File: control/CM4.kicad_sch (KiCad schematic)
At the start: 1 part

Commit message: Cleanup/organization
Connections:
- net +5V: now reaches Module1.77 (+5v_(Input)), Module1.79 (+5v_(Input)), Module1.81 (+5v_(Input)), Module1.83 (+5v_(Input)), Module1.85 (+5v_(Input)), Module1.87 (+5v_(Input))
- net +3V3: now reaches Module1.84 (+3.3v_(Output)), Module1.86 (+3.3v_(Output))
- net +1V8: now reaches Module1.88 (+1.8v_(Output)), Module1.90 (+1.8v_(Output))
- no-connect marks 73 -> 86

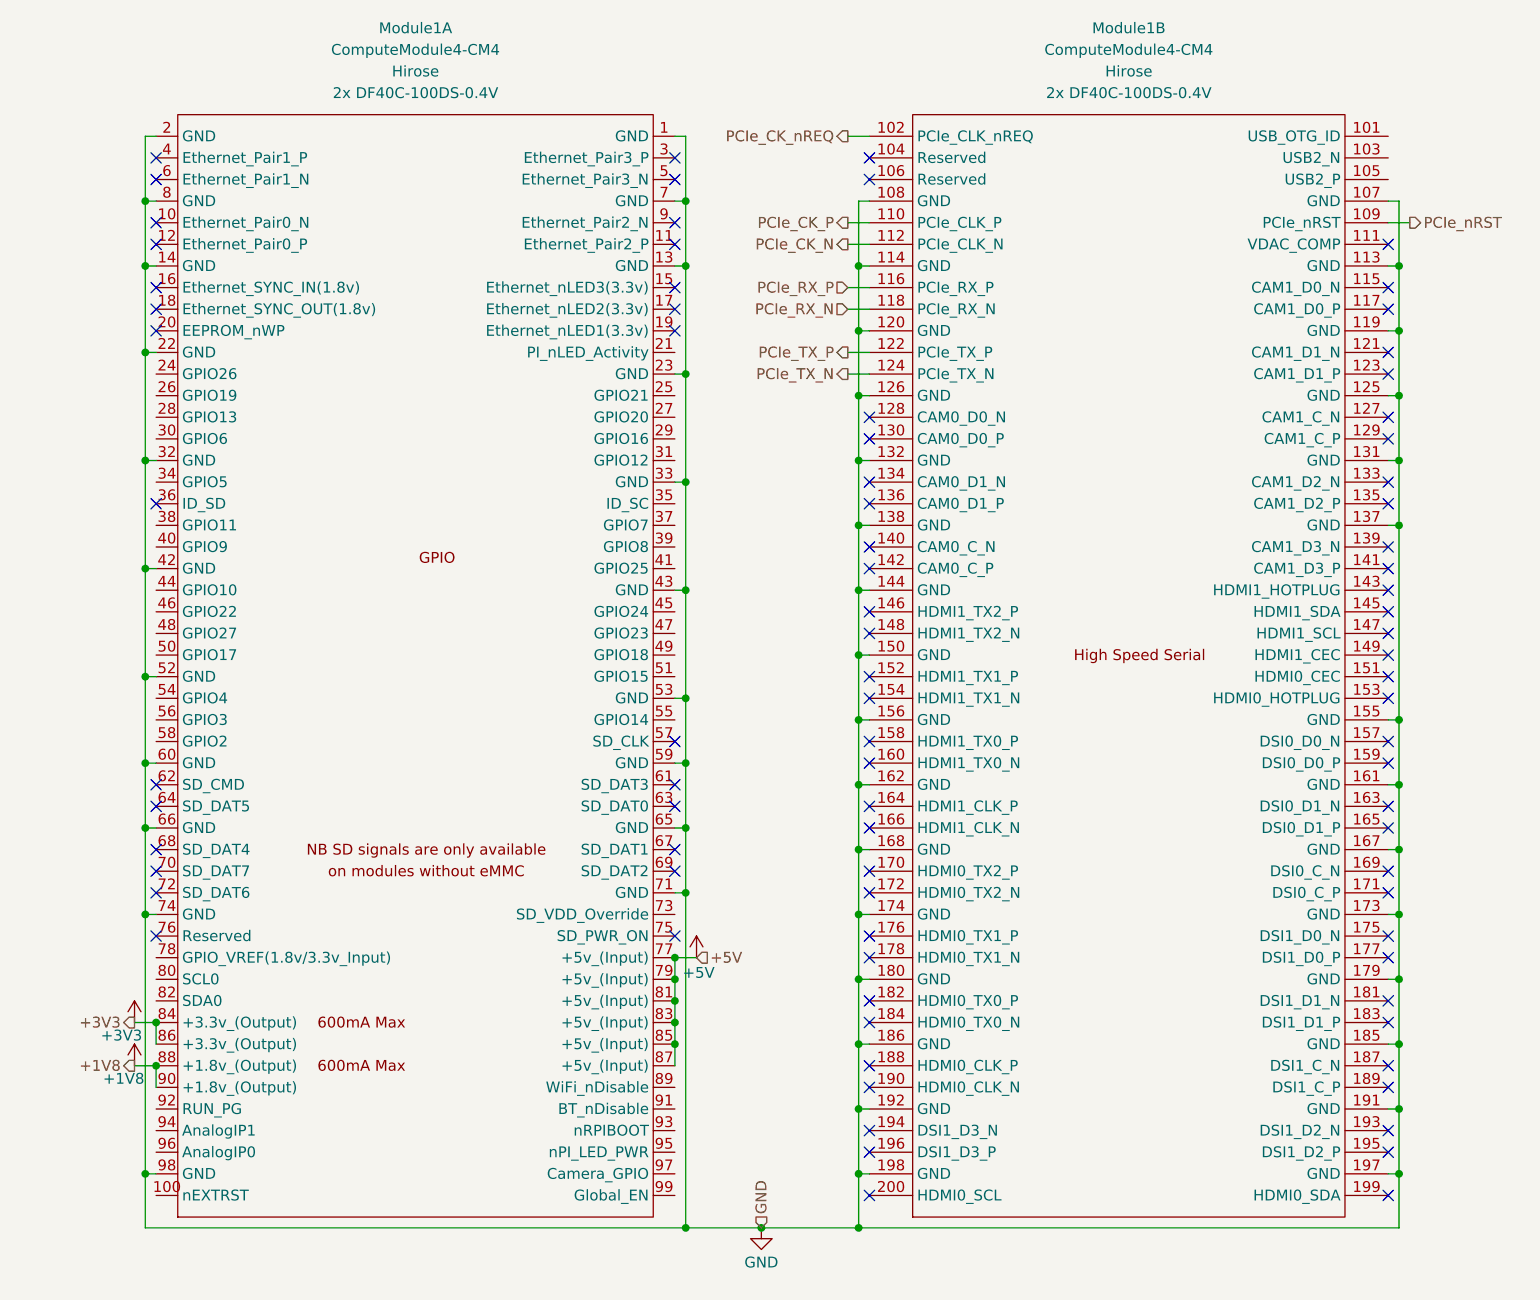
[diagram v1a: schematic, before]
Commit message: Component selection and BME280 cleanup
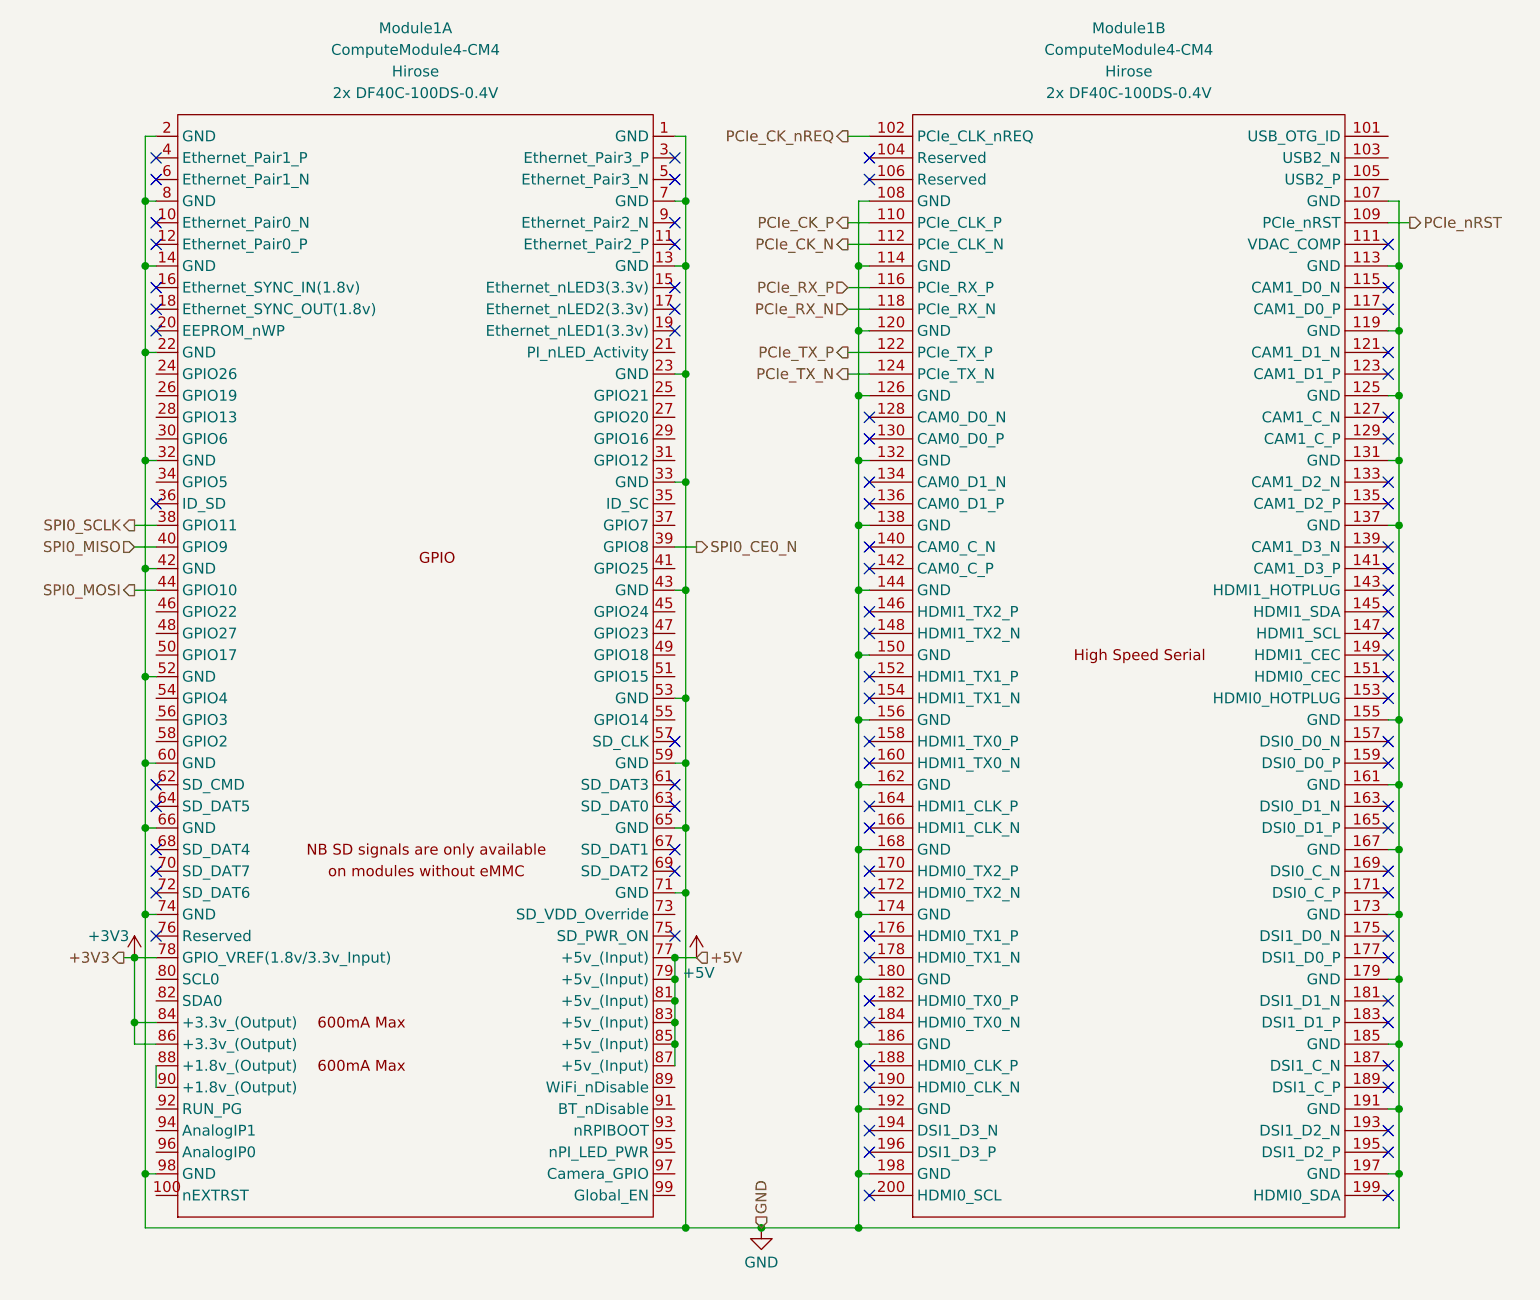
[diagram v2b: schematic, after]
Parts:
- Module1: PN CM4104000 -> SC0671
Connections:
- net +3V3: now also Module1.78 (GPIO_VREF(1.8v/3.3v_Input))
- net SPI0_SCLK: now reaches Module1.38 (GPIO11)
- net SPI0_CE0_N: now reaches Module1.39 (GPIO8)
- net SPI0_MISO: now reaches Module1.40 (GPIO9)
- net SPI0_MOSI: now reaches Module1.44 (GPIO10)
- net +1V8: no longer names the net of Module1.88 (+1.8v_(Output)), Module1.90 (+1.8v_(Output))
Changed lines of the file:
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@@
+	)
+	(junction
+		(at 40.64 133.35)
+		(diameter 0)
+		(color 0 0 0 0)
 	)
 	(junction
@@
 	)
 	(junction
-		(at 43.18 133.35)
-		(diameter 0)
-		(color 0 0 0 0)
-	)
-	(junction
 		(at 125.73 44.45)
 		(diameter 0)
@@
 	)
 	(junction
+		(at 40.64 125.73)
+		(diameter 0)
+		(color 0 0 0 0)
+	)
+	(junction
 		(at 105.41 95.25)
 		(diameter 0)
@@
 	)
 	(junction
-		(at 43.18 138.43)
-		(diameter 0)
-		(color 0 0 0 0)
-	)
-	(junction
 		(at 41.91 151.13)
 		(diameter 0)
@@
 	(wire
 		(pts
+			(xy 40.64 133.35) (xy 43.18 133.35)
+		)
+		(stroke
+			(width 0)
+			(type default)
+		)
+	)
+	(wire
+		(pts
 			(xy 104.14 95.25) (xy 105.41 95.25)
 		)
@@
 	(wire
 		(pts
+			(xy 40.64 82.55) (xy 43.18 82.55)
+		)
+		(stroke
+			(width 0)
+			(type default)
+		)
+	)
+	(wire
+		(pts
 			(xy 104.14 44.45) (xy 105.41 44.45)
 		)
@@
 	(wire
 		(pts
+			(xy 39.37 125.73) (xy 40.64 125.73)
+		)
+		(stroke
+			(width 0)
+			(type default)
+		)
+	)
+	(wire
+		(pts
 			(xy 189.23 59.69) (xy 187.96 59.69)
 		)
@@
 	(wire
 		(pts
+			(xy 40.64 125.73) (xy 43.18 125.73)
+		)
+		(stroke
+			(width 0)
+			(type default)
+		)
+	)
+	(wire
+		(pts
 			(xy 41.91 157.48) (xy 41.91 151.13)
 		)
@@
 	(wire
 		(pts
-			(xy 41.91 151.13) (xy 41.91 120.65)
-		)
-		(stroke
-			(width 0)
-			(type default)
-		)
-	)
-	(wire
-		(pts
 			(xy 114.3 157.48) (xy 105.41 157.48)
 		)
@@
 	(wire
 		(pts
+			(xy 40.64 77.47) (xy 43.18 77.47)
+		)
+		(stroke
+			(width 0)
+			(type default)
+		)
+	)
+	(wire
+		(pts
 			(xy 127 120.65) (xy 125.73 120.65)
 		)
@@
 	(wire
 		(pts
-			(xy 40.64 138.43) (xy 43.18 138.43)
-		)
-		(stroke
-			(width 0)
-			(type default)
-		)
-	)
-	(wire
-		(pts
 			(xy 125.73 67.31) (xy 125.73 59.69)
 		)
@@
 	(wire
 		(pts
+			(xy 104.14 77.47) (xy 106.68 77.47)
+		)
+		(stroke
+			(width 0)
+			(type default)
+		)
+	)
+	(wire
+		(pts
 			(xy 125.73 143.51) (xy 127 143.51)
 		)
@@
 	(wire
 		(pts
+			(xy 40.64 74.93) (xy 43.18 74.93)
+		)
+		(stroke
+			(width 0)
+			(type default)
+		)
+	)
+	(wire
+		(pts
 			(xy 104.14 135.89) (xy 104.14 138.43)
 		)
@@
 	(wire
 		(pts
-			(xy 43.18 133.35) (xy 43.18 135.89)
+			(xy 40.64 133.35) (xy 40.64 135.89)
 		)
 		(stroke
@@
 	(wire
 		(pts
+			(xy 40.64 135.89) (xy 43.18 135.89)
+		)
+		(stroke
+			(width 0)
+			(type default)
+		)
+	)
+	(wire
+		(pts
 			(xy 125.73 143.51) (xy 125.73 151.13)
 		)
@@
 	(wire
 		(pts
-			(xy 40.64 133.35) (xy 43.18 133.35)
-		)
-		(stroke
-			(width 0)
-			(type default)
-		)
-	)
-	(wire
-		(pts
 			(xy 127 128.27) (xy 125.73 128.27)
 		)
@@
 	(wire
 		(pts
+			(xy 41.91 120.65) (xy 41.91 151.13)
+		)
+		(stroke
+			(width 0)
+			(type default)
+		)
+	)
+	(wire
+		(pts
 			(xy 125.73 74.93) (xy 125.73 67.31)
 		)
@@
 		(pts
 			(xy 105.41 36.83) (xy 104.14 36.83)
+		)
+		(stroke
+			(width 0)
+			(type default)
+		)
+	)
+	(wire
+		(pts
+			(xy 40.64 133.35) (xy 40.64 125.73)
 		)
 		(stroke
@@
 		)
 	)
+	(hierarchical_label "SPI0_MOSI"
+		(shape output)
+		(at 40.64 82.55 180)
+		(fields_autoplaced yes)
+		(effects
+			(font
+				(size 1.27 1.27)
+			)
+			(justify right)
+		)
+	)
+	(hierarchical_label "SPI0_CE0_N"
+		(shape output)
+		(at 106.68 77.47 0)
+		(fields_autoplaced yes)
+		(effects
+			(font
+				(size 1.27 1.27)
+			)
+			(justify left)
+		)
+	)
 	(hierarchical_label "PCIe_RX_P"
 		(shape input)
@@
 		)
 	)
+	(hierarchical_label "SPI0_MISO"
+		(shape input)
+		(at 40.64 77.47 180)
+		(fields_autoplaced yes)
+		(effects
+			(font
+				(size 1.27 1.27)
+			)
+			(justify right)
+		)
+	)
 	(hierarchical_label "PCIe_CK_P"
 		(shape output)
@@
 		)
 	)
+	(hierarchical_label "SPI0_SCLK"
+		(shape output)
+		(at 40.64 74.93 180)
+		(fields_autoplaced yes)
+		(effects
+			(font
+				(size 1.27 1.27)
+			)
+			(justify right)
+		)
+	)
 	(hierarchical_label "PCIe_CK_nREQ"
 		(shape output)
@@
 		)
 	)
-	(hierarchical_label "+1V8"
-		(shape output)
-		(at 40.64 138.43 180)
-		(fields_autoplaced yes)
-		(effects
-			(font
-				(size 1.27 1.27)
-			)
-			(justify right)
-		)
-	)
 	(hierarchical_label "+5V"
 		(shape input)
@@
 	(hierarchical_label "+3V3"
 		(shape output)
-		(at 40.64 133.35 180)
+		(at 39.37 125.73 180)
 		(fields_autoplaced yes)
 		(effects
@@
 			)
 		)
-		(property "PN" "CM4104000"
+		(property "PN" "SC0671"
 			(at 76.2 85.09 0)
 			(effects
@@
 	(symbol
 		(lib_id "power:+3V3")
-		(at 40.64 133.35 0)
+		(at 40.64 125.73 0)
 		(unit 1)
 		(exclude_from_sim no)
@@
 		(dnp no)
 		(property "Reference" "#PWR027"
-			(at 40.64 137.16 0)
+			(at 40.64 129.54 0)
 			(effects
 				(font
@@
 		)
 		(property "Value" "+3V3"
-			(at 39.116 134.874 0)
+			(at 37.592 123.19 0)
 			(effects
 				(font
@@
 		)
 		(property "Footprint" ""
-			(at 40.64 133.35 0)
+			(at 40.64 125.73 0)
 			(effects
 				(font
@@
 		)
 		(property "Datasheet" ""
-			(at 40.64 133.35 0)
+			(at 40.64 125.73 0)
 			(effects
 				(font
@@
 		)
 		(property "Description" "Power symbol creates a global label with name \"+3V3\""
-			(at 40.64 133.35 0)
+			(at 40.64 125.73 0)
 			(effects
 				(font
@@
 				(path "/f45f1ed7-9099-407f-b6ad-6cac15e7865f/5e58b04a-ae38-42c8-ade5-91d029711ef9"
 					(reference "#PWR025")
-					(unit 1)
-				)
-			)
-		)
-	)
-	(symbol
-		(lib_id "power:+1V8")
-		(at 40.64 138.43 0)
-		(unit 1)
-		(exclude_from_sim no)
-		(in_bom yes)
-		(on_board yes)
-		(dnp no)
-		(property "Reference" "#PWR028"
-			(at 40.64 142.24 0)
-			(effects
-				(font
-					(size 1.27 1.27)
-				)
-				(hide yes)
-			)
-		)
-		(property "Value" "+1V8"
-			(at 39.37 139.954 0)
-			(effects
-				(font
-					(size 1.27 1.27)
-				)
-			)
-		)
-		(property "Footprint" ""
-			(at 40.64 138.43 0)
-			(effects
-				(font
-					(size 1.27 1.27)
-				)
-				(hide yes)
-			)
-		)
-		(property "Datasheet" ""
-			(at 40.64 138.43 0)
-			(effects
-				(font
-					(size 1.27 1.27)
-				)
-				(hide yes)
-			)
-		)
-		(property "Description" "Power symbol creates a global label with name \"+1V8\""
-			(at 40.64 138.43 0)
-			(effects
-				(font
-					(size 1.27 1.27)
-				)
-				(hide yes)
-			)
-		)
-		(pin "1"
-		)
-		(instances
-			(project ""
-				(path "/f45f1ed7-9099-407f-b6ad-6cac15e7865f/5e58b04a-ae38-42c8-ade5-91d029711ef9"
-					(reference "#PWR028")
 					(unit 1)
 				)
@@
 			)
 		)
-		(property "PN" "CM4104000"
+		(property "PN" "SC0671"
 			(at 17.78 90.17 0)
 			(effects

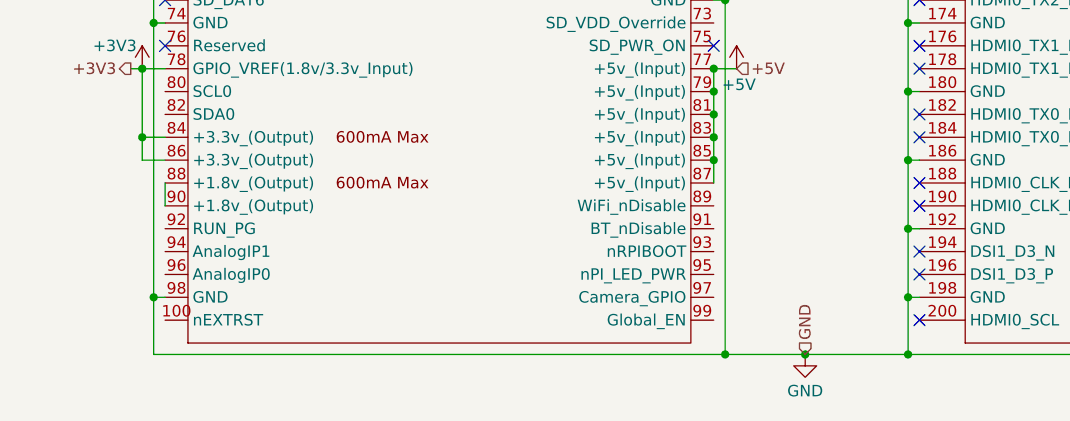
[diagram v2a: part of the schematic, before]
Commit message: decoupling cap
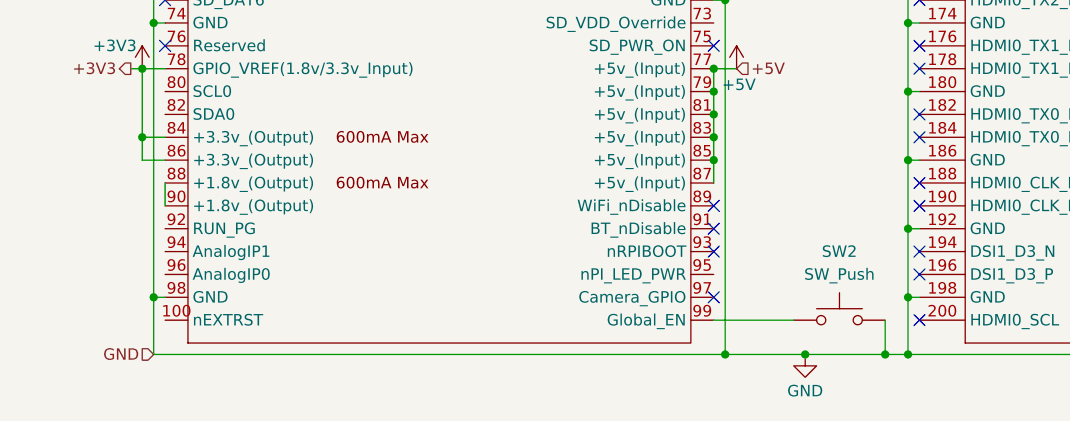
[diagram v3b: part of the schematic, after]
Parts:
- added SW2: SW_Push, symbol Switch:SW_Push
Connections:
- net GND: now also SW2.2
- net at Module1.99 (Global_EN): now also SW2.1
- no-connect marks 86 -> 90
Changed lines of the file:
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@@
+	)
+	(junction
+		(at 123.19 157.48)
+		(diameter 0)
+		(color 0 0 0 0)
 	)
 	(junction
@@
 	)
 	(no_connect
+		(at 104.14 151.13)
+	)
+	(no_connect
 		(at 127 107.95)
 	)
@@
 	)
 	(no_connect
+		(at 104.14 140.97)
+	)
+	(no_connect
 		(at 43.18 72.39)
 	)
@@
 	)
 	(no_connect
+		(at 104.14 146.05)
+	)
+	(no_connect
 		(at 187.96 87.63)
 	)
@@
 	)
 	(no_connect
+		(at 104.14 143.51)
+	)
+	(no_connect
 		(at 127 133.35)
 	)
@@
 	(wire
 		(pts
-			(xy 114.3 157.48) (xy 125.73 157.48)
+			(xy 114.3 157.48) (xy 123.19 157.48)
+		)
+		(stroke
+			(width 0)
+			(type default)
+		)
+	)
+	(wire
+		(pts
+			(xy 123.19 157.48) (xy 125.73 157.48)
 		)
 		(stroke
@@
 	(wire
 		(pts
+			(xy 123.19 153.67) (xy 123.19 157.48)
+		)
+		(stroke
+			(width 0)
+			(type default)
+		)
+	)
+	(wire
+		(pts
 			(xy 125.73 157.48) (xy 189.23 157.48)
 		)
@@
 		(pts
 			(xy 105.41 57.15) (xy 105.41 44.45)
+		)
+		(stroke
+			(width 0)
+			(type default)
+		)
+	)
+	(wire
+		(pts
+			(xy 104.14 153.67) (xy 113.03 153.67)
 		)
 		(stroke
@@
 	(hierarchical_label "GND"
 		(shape input)
-		(at 114.3 157.48 90)
+		(at 41.91 157.48 180)
 		(fields_autoplaced yes)
 		(effects
@@
 				(size 1.27 1.27)
 			)
-			(justify left)
+			(justify right)
 		)
 	)
@@
 					(unit 1)
 				)
+			)
+		)
+	)
+	(symbol
+		(lib_id "Switch:SW_Push")
+		(at 118.11 153.67 0)
+		(unit 1)
+		(exclude_from_sim no)
+		(in_bom yes)
+		(on_board yes)
+		(dnp no)
+		(fields_autoplaced yes)
+		(property "Reference" "SW2"
+			(at 118.11 146.05 0)
+			(effects
+				(font
+					(size 1.27 1.27)
+				)
+			)
+		)
+		(property "Value" "SW_Push"
+			(at 118.11 148.59 0)
+			(effects
+				(font
+					(size 1.27 1.27)
+				)
+			)
+		)
+		(property "Footprint" ""
+			(at 118.11 148.59 0)
+			(effects
+				(font
+					(size 1.27 1.27)
+				)
+				(hide yes)
+			)
+		)
+		(property "Datasheet" "~"
+			(at 118.11 148.59 0)
+			(effects
+				(font
+					(size 1.27 1.27)
+				)
+				(hide yes)
+			)
+		)
+		(property "Description" "Push button switch, generic, two pins"
+			(at 118.11 153.67 0)
+			(effects
+				(font
+					(size 1.27 1.27)
+				)
+				(hide yes)
+			)
+		)
+		(pin "1"
+		)
+		(pin "2"
+		)
+		(instances
+			(project ""
+				(path "/f45f1ed7-9099-407f-b6ad-6cac15e7865f/5e58b04a-ae38-42c8-ade5-91d029711ef9"
+					(reference "SW2")
+					(unit 1)
+				)
